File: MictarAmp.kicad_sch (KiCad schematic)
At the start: 12 parts, among them J1 AudioJack3, J2 AudioJack4, J3 AudioJack2, J4 AudioJack3, SW1 SW_Push_SPDT, SW2 SW_Push_SPDT, U1 LM386, U2 TP4056

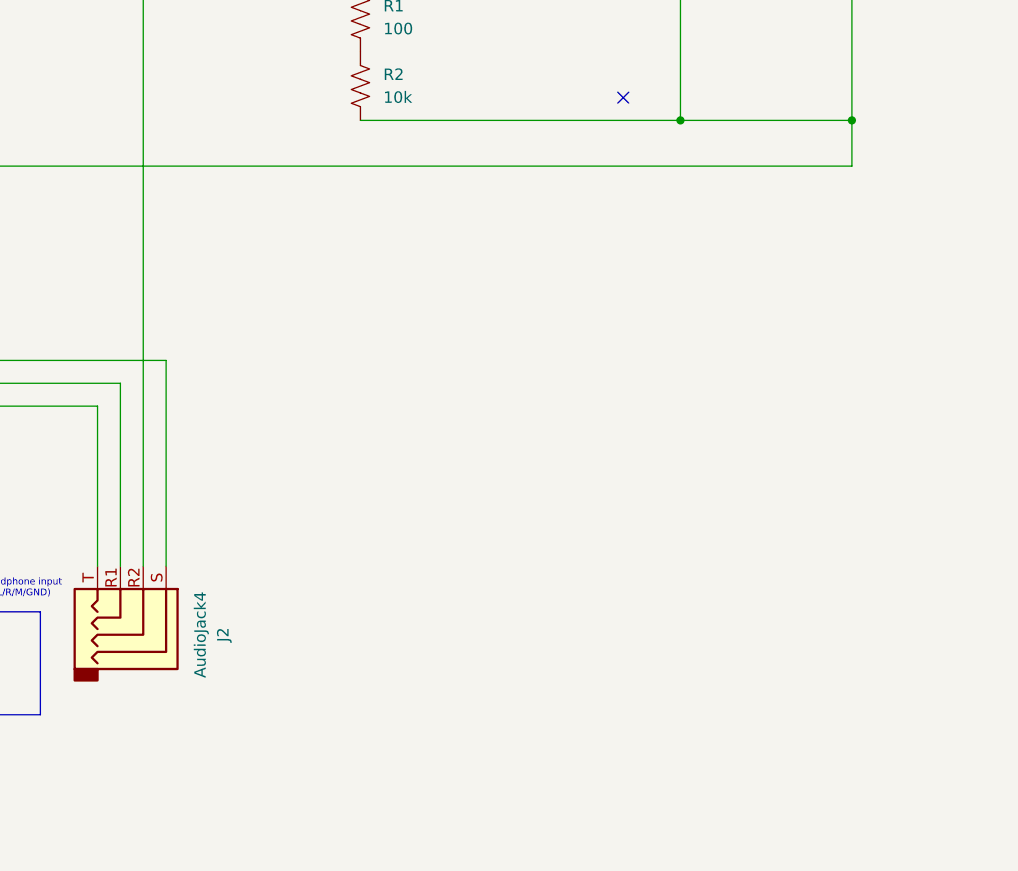
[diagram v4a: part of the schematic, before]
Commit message: added central ground
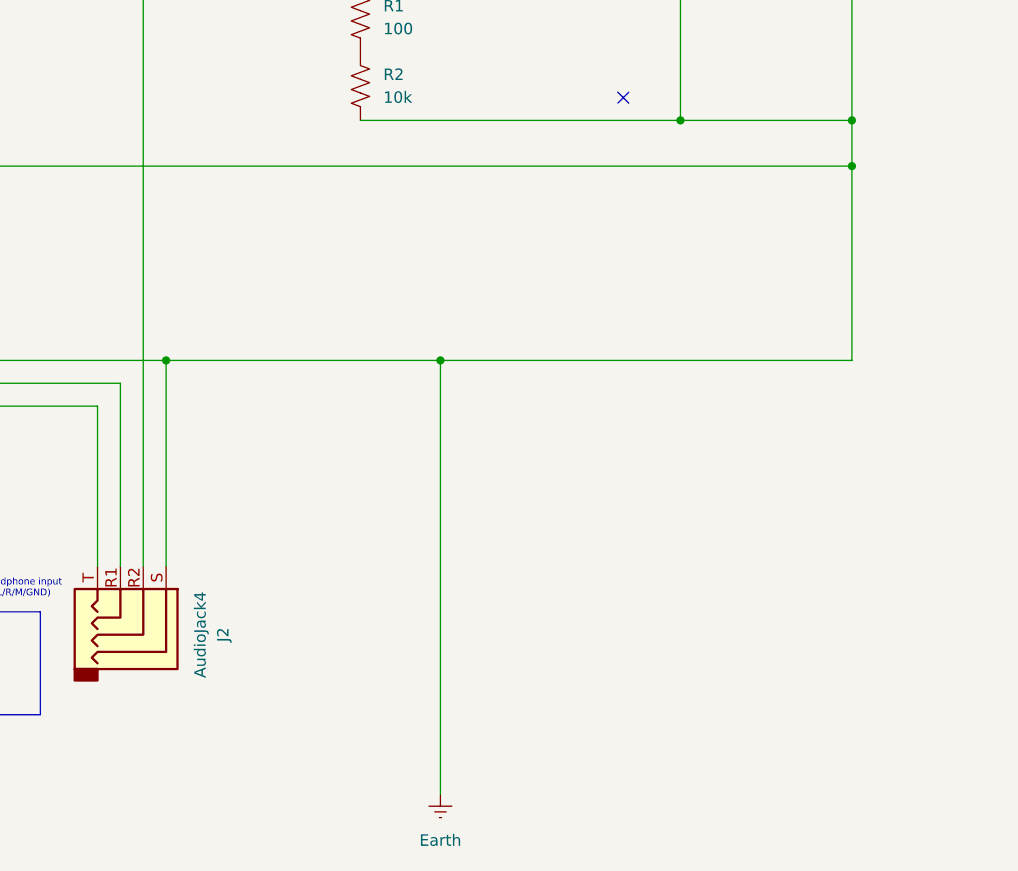
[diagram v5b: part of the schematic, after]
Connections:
- net Earth: now reaches J4.S, R2.1, SW1.2 (B), U1.4 (GND)
- net Earth: now also J1.S, J2.S
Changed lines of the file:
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@@
 	(paper "A4")
 	(junction
+		(at 160.02 137.16)
+		(diameter 0)
+		(color 0 0 0 0)
+	)
+	(junction
 		(at 186.69 110.49)
 		(diameter 0)
@@
 	)
 	(junction
+		(at 129.54 137.16)
+		(diameter 0)
+		(color 0 0 0 0)
+	)
+	(junction
+		(at 205.74 115.57)
+		(diameter 0)
+		(color 0 0 0 0)
+	)
+	(junction
 		(at 151.13 95.25)
 		(diameter 0)
@@
 	(wire
 		(pts
+			(xy 129.54 137.16) (xy 160.02 137.16)
+		)
+		(stroke
+			(width 0)
+			(type default)
+		)
+	)
+	(wire
+		(pts
+			(xy 160.02 137.16) (xy 205.74 137.16)
+		)
+		(stroke
+			(width 0)
+			(type default)
+		)
+	)
+	(wire
+		(pts
 			(xy 95.25 90.17) (xy 95.25 118.11)
 		)
@@
 	(wire
 		(pts
+			(xy 205.74 115.57) (xy 205.74 137.16)
+		)
+		(stroke
+			(width 0)
+			(type default)
+		)
+	)
+	(wire
+		(pts
+			(xy 160.02 137.16) (xy 160.02 185.42)
+		)
+		(stroke
+			(width 0)
+			(type default)
+		)
+	)
+	(wire
+		(pts
 			(xy 165.1 95.25) (xy 151.13 95.25)
 		)
@@
 					(unit 1)
 				)
+			)
+		)
+	)
+	(symbol
+		(lib_id "power:Earth")
+		(at 160.02 185.42 0)
+		(unit 1)
+		(exclude_from_sim no)
+		(in_bom yes)
+		(on_board yes)
+		(dnp no)
+		(fields_autoplaced yes)
+		(property "Reference" "#PWR01"
+			(at 160.02 191.77 0)
+			(effects
+				(font
+					(size 1.27 1.27)
+				)
+				(hide yes)
+			)
+		)
+		(property "Value" "Earth"
+			(at 160.02 190.5 0)
+			(effects
+				(font
+					(size 1.27 1.27)
+				)
+			)
+		)
+		(property "Footprint" ""
+			(at 160.02 185.42 0)
+			(effects
+				(font
+					(size 1.27 1.27)
+				)
+				(hide yes)
+			)
+		)
+		(property "Datasheet" "~"
+			(at 160.02 185.42 0)
+			(effects
+				(font
+					(size 1.27 1.27)
+				)
+				(hide yes)
+			)
+		)
+		(property "Description" "Power symbol creates a global label with name \"Earth\""
+			(at 160.02 185.42 0)
+			(effects
+				(font
+					(size 1.27 1.27)
+				)
+				(hide yes)
+			)
+		)
+		(pin "1"
+		)
+		(instances
+			(project ""
+				(path "/baae048e-34bc-426f-a829-0c3587a71fd5"
+					(reference "#PWR01")
+					(unit 1)
+				)
